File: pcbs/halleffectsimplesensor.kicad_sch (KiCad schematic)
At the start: 3 parts, among them J10 Conn_01x04_Pin, U6 BME680

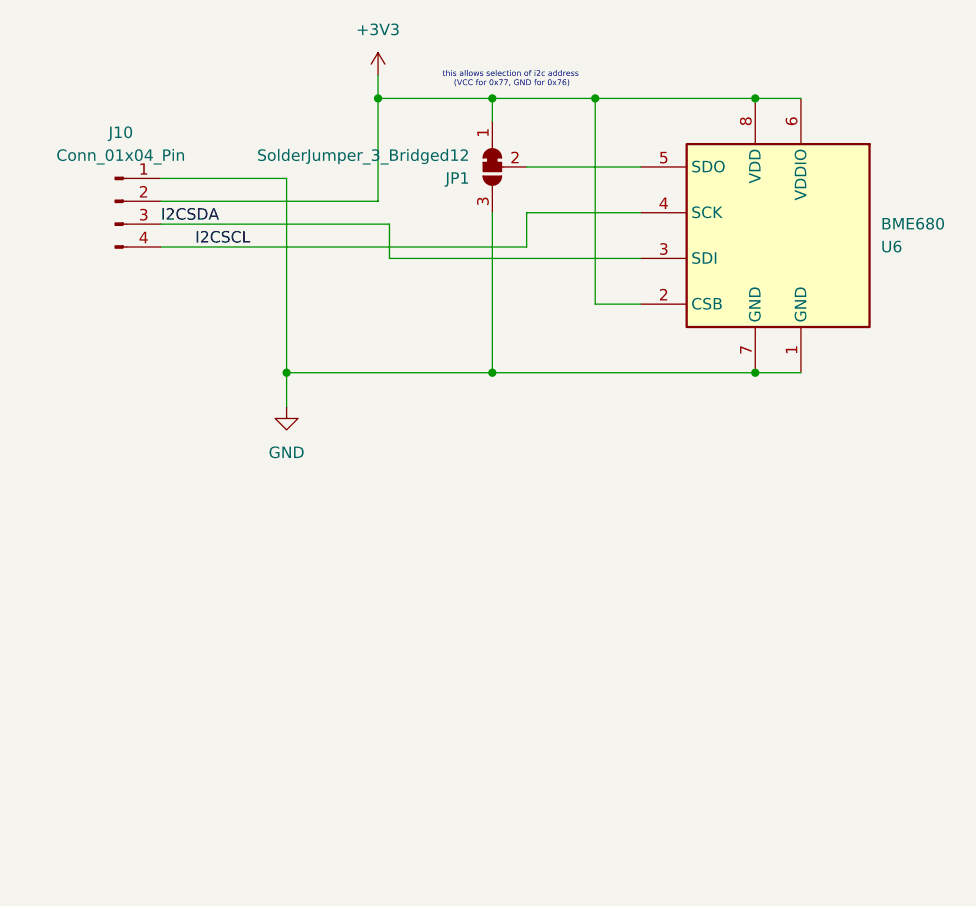
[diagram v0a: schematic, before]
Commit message: add ld2450, recreate simple hall effect sensor, add ssd1306 display
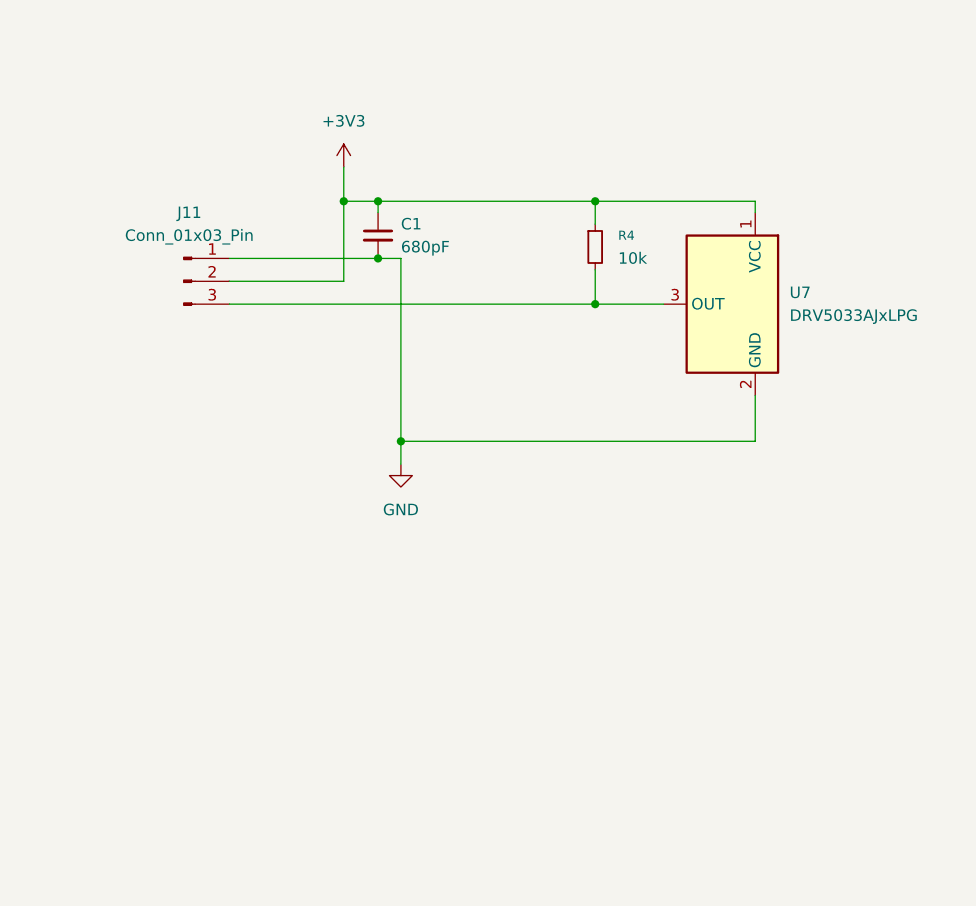
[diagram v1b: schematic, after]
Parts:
- removed J10: Conn_01x04_Pin, symbol Connector:Conn_01x04_Pin
- removed JP1: SolderJumper_3_Bridged12, symbol Jumper:SolderJumper_3_Bridged12
- removed U6: BME680, Package_LGA:Bosch_LGA-8_3x3mm_P0.8mm_ClockwisePinNumbering, symbol Sensor:BME680
- added C1: 680pF, symbol Device:C_Small
- added J11: Conn_01x03_Pin, symbol Connector:Conn_01x03_Pin
- added R4: 10k, symbol Device:R_Small
- added U7: DRV5033AJxLPG, Package_TO_SOT_THT:TO-92_Inline, symbol Sensor_Magnetic:DRV5033AJxLPG
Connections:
- net +3V3: now also C1.1, J11.2 (Pin_2), R4.1, U7.1 (VCC)
- net GND: now also C1.2, J11.1 (Pin_1), U7.2 (GND)
- new net: J11.3 (Pin_3), R4.2, U7.3 (OUT)
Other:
- note removed: "this allows selection of i2c address (VCC for 0x77, GND for 0x76)"

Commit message: try to fix kicad weirdness
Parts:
- renumbered J11 to J8, R4 to R3, U7 to U6
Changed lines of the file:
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@@
 		(dnp no)
 		(fields_autoplaced yes)
-		(property "Reference" "U7"
+		(property "Reference" "U6"
 			(at 129.54 67.3099 0)
 			(show_name no)
@@
 			(project "monstera"
 				(path "/86ba5bd3-984c-4b85-bed3-e21d59b4241f"
-					(reference "U7")
+					(reference "U6")
 					(unit 1)
 				)
@@
 		(dnp no)
 		(fields_autoplaced yes)
-		(property "Reference" "#PWR017"
+		(property "Reference" "#PWR016"
 			(at 80.01 57.15 0)
 			(hide yes)
@@
 			(project "monstera"
 				(path "/86ba5bd3-984c-4b85-bed3-e21d59b4241f"
-					(reference "#PWR017")
+					(reference "#PWR016")
 					(unit 1)
 				)
@@
 		(dnp no)
 		(fields_autoplaced yes)
-		(property "Reference" "#PWR019"
+		(property "Reference" "#PWR017"
 			(at 86.36 92.71 0)
 			(hide yes)
@@
 			(project "monstera"
 				(path "/86ba5bd3-984c-4b85-bed3-e21d59b4241f"
-					(reference "#PWR019")
+					(reference "#PWR017")
 					(unit 1)
 				)
@@
 		(dnp no)
 		(fields_autoplaced yes)
-		(property "Reference" "J11"
+		(property "Reference" "J8"
 			(at 62.865 58.42 0)
 			(show_name no)
@@
 			(project "monstera"
 				(path "/86ba5bd3-984c-4b85-bed3-e21d59b4241f"
-					(reference "J11")
+					(reference "J8")
 					(unit 1)
 				)
@@
 		(dnp no)
 		(fields_autoplaced yes)
-		(property "Reference" "R4"
+		(property "Reference" "R3"
 			(at 110.49 60.9599 0)
 			(show_name no)
@@
 			(project "monstera"
 				(path "/86ba5bd3-984c-4b85-bed3-e21d59b4241f"
-					(reference "R4")
-					(unit 1)
-				)
+					(reference "R3")
+					(unit 1)
+				)

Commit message: make sensor pcbs
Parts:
- added H1, H2, H3, H4: MountingHole, symbol Mechanical:MountingHole
- C1: footprint (none) -> Capacitor_SMD:C_0805_2012Metric_Pad1.18x1.45mm_HandSolder
- J8: footprint (none) -> Connector_JST:JST_PH_S3B-PH-K_1x03_P2.00mm_Horizontal
- R3: footprint (none) -> Resistor_SMD:R_0805_2012Metric_Pad1.20x1.40mm_HandSolder
